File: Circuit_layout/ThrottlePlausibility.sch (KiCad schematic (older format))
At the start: 63 parts, among them SW1 TS5A3159-Q1, U1 ACPL-C870, U2 LM7810CT, U3 LM7805CT, U5 LM7332, U6 LM339, U8 74ACT11030

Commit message: added cap. info. for orders
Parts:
- removed C? (x9): 0.1u, symbol C
- added C? (x7): 0.1u, Capacitors_SMD:C_0805_HandSoldering, symbol C
- C?: footprint (none) -> Capacitors_SMD:C_0805_HandSoldering
- C?: footprint (none) -> Capacitors_SMD:C_0805_HandSoldering; Digikey P/N (none) -> 399-1168-1-ND; Man P/N (none) -> C0805C104K3RACTU; URL (none) -> http://www.digikey.com/product-detail/en/kemet/C0805C104K3R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
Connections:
- wire segments 168 -> 163
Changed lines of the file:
@@
 EESchema Schematic File Version 2
 LIBS:Circuit_layout-rescue
-LIBS:TSI_KiCad_Lib
 LIBS:TSI_HV_Isolater-cache
 LIBS:74xgxx
@@
 Wire Wire Line
 	5200 3700 5850 3700
-Wire Wire Line
-	5200 3900 5850 3900
-$Comp
-L C C?
-U 1 1 58ADD879
-P 5650 4200
-F 0 "C?" H 5675 4300 50  0000 L CNN
-F 1 "0.1u" H 5675 4100 50  0000 L CNN
-F 2 "" H 5688 4050 50  0000 C CNN
-F 3 "" H 5650 4200 50  0000 C CNN
-	1    5650 4200
-	1    0    0    -1
-$EndComp
-$Comp
-L C C?
-U 1 1 58ADD957
-P 5650 3400
-F 0 "C?" H 5675 3500 50  0000 L CNN
-F 1 "0.1u" H 5675 3300 50  0000 L CNN
-F 2 "" H 5688 3250 50  0000 C CNN
-F 3 "" H 5650 3400 50  0000 C CNN
-	1    5650 3400
-	1    0    0    -1
-$EndComp
 Text HLabel 3200 1700 0    60   Input ~ 0
 BP
@@
 F 0 "C?" H 11975 3600 50  0000 L CNN
 F 1 "DNP" H 11975 3400 50  0000 L CNN
-F 2 "" H 11988 3350 50  0000 C CNN
+F 2 "Capacitors_SMD:C_0805_HandSoldering" H 11988 3350 50  0001 C CNN
 F 3 "" H 11950 3500 50  0000 C CNN
 	1    11950 3500
@@
 	6150 3700 6400 3700
 Wire Wire Line
-	5650 3700 5650 3550
-Connection ~ 5650 3700
-Wire Wire Line
-	5650 4050 5650 3900
-Connection ~ 5650 3900
-Wire Wire Line
-	5650 3100 5650 3250
-Wire Wire Line
 	6300 3700 6300 3550
 Connection ~ 6300 3700
 Wire Wire Line
 	6300 3250 6300 3150
-Wire Wire Line
-	6300 3150 5650 3150
-Connection ~ 5650 3150
 $Comp
 L MCP6004 U?
@@
 F 0 "C?" H 3625 6850 50  0000 L CNN
 F 1 "0.1u" H 3625 6650 50  0000 L CNN
-F 2 "" H 3638 6600 50  0000 C CNN
-F 3 "" H 3600 6750 50  0000 C CNN
+F 2 "Capacitors_SMD:C_0805_HandSoldering" H 3638 6600 50  0001 C CNN
+F 3 "http://www.kemet.com/Lists/ProductCatalog/Attachments/53/KEM_C1002_X7R_SMD.pdf" H 3600 6750 50  0001 C CNN
+F 4 "399-1168-1-ND" H 3600 6750 60  0001 C CNN "Digikey P/N"
+F 5 "http://www.digikey.com/product-detail/en/kemet/C0805C104K3RACTU/399-1168-1-ND/411443" H 3600 6750 60  0001 C CNN "URL"
+F 6 "C0805C104K3RACTU" H 3600 6750 60  0001 C CNN "Man P/N"
 	1    3600 6750
-	1    0    0    -1
-$EndComp
-$Comp
-L C C?
-U 1 1 58AF6374
-P 3750 5950
-F 0 "C?" H 3775 6050 50  0000 L CNN
-F 1 "0.1u" H 3775 5850 50  0000 L CNN
-F 2 "" H 3788 5800 50  0000 C CNN
-F 3 "" H 3750 5950 50  0000 C CNN
-	1    3750 5950
 	1    0    0    -1
 $EndComp
@@
 	1    0    0    -1
 $EndComp
-Wire Wire Line
-	5650 4350 5650 4400
-$Comp
-L GND #PWR?
-U 1 1 58B314D0
-P 5650 4400
-F 0 "#PWR?" H 5650 4150 50  0001 C CNN
-F 1 "GND" H 5650 4250 50  0000 C CNN
-F 2 "" H 5650 4400 50  0000 C CNN
-F 3 "" H 5650 4400 50  0000 C CNN
-	1    5650 4400
-	1    0    0    -1
-$EndComp
 $Comp
 L GND #PWR?
 U 1 1 58B31589
-P 5650 3100
-F 0 "#PWR?" H 5650 2850 50  0001 C CNN
-F 1 "GND" H 5650 2950 50  0000 C CNN
-F 2 "" H 5650 3100 50  0000 C CNN
-F 3 "" H 5650 3100 50  0000 C CNN
-	1    5650 3100
+P 6300 3150
+F 0 "#PWR?" H 6300 2900 50  0001 C CNN
+F 1 "GND" H 6300 3000 50  0000 C CNN
+F 2 "" H 6300 3150 50  0000 C CNN
+F 3 "" H 6300 3150 50  0000 C CNN
+	1    6300 3150
 	1    0    0    1
 $EndComp
@@
 $EndComp
 $Comp
-L C C?
-U 1 1 58B3EF6F
-P 1650 2600
-F 0 "C?" H 1675 2700 50  0000 L CNN
-F 1 "0.1u" H 1675 2500 50  0000 L CNN
-F 2 "" H 1688 2450 50  0000 C CNN
-F 3 "" H 1650 2600 50  0000 C CNN
-	1    1650 2600
-	1    0    0    -1
-$EndComp
-$Comp
 L GND #PWR?
 U 1 1 58B3F616
@@
 Wire Wire Line
 	1550 1600 1850 1600
-$Comp
-L C C?
-U 1 1 58B403F1
-P 1650 1000
-F 0 "C?" H 1675 1100 50  0000 L CNN
-F 1 "0.1u" H 1675 900 50  0000 L CNN
-F 2 "" H 1688 850 50  0000 C CNN
-F 3 "" H 1650 1000 50  0000 C CNN
-	1    1650 1000
-	1    0    0    -1
-$EndComp
-$Comp
-L C C?
-U 1 1 58B404F5
-P 1650 1750
-F 0 "C?" H 1675 1850 50  0000 L CNN
-F 1 "0.1u" H 1675 1650 50  0000 L CNN
-F 2 "" H 1688 1600 50  0000 C CNN
-F 3 "" H 1650 1750 50  0000 C CNN
-	1    1650 1750
-	1    0    0    -1
-$EndComp
 Connection ~ 1650 1600
 Connection ~ 1650 850
@@
 Wire Wire Line
 	1550 3150 1850 3150
-$Comp
-L C C?
-U 1 1 58B47FEA
-P 1650 3300
-F 0 "C?" H 1675 3400 50  0000 L CNN
-F 1 "0.1u" H 1675 3200 50  0000 L CNN
-F 2 "" H 1688 3150 50  0000 C CNN
-F 3 "" H 1650 3300 50  0000 C CNN
-	1    1650 3300
-	1    0    0    -1
-$EndComp
 Connection ~ 1650 3150
 Text Label 1850 3150 0    60   ~ 0
@@
 Wire Wire Line
 	1550 3800 1850 3800
-$Comp
-L C C?
-U 1 1 58B4811B
-P 1650 3950
-F 0 "C?" H 1675 4050 50  0000 L CNN
-F 1 "0.1u" H 1675 3850 50  0000 L CNN
-F 2 "" H 1688 3800 50  0000 C CNN
-F 3 "" H 1650 3950 50  0000 C CNN
-	1    1650 3950
-	1    0    0    -1
-$EndComp
 Connection ~ 1650 3800
 Text Label 1850 3800 0    60   ~ 0
@@
 F 3 "" H 1650 4100 50  0000 C CNN
 	1    1650 4100
-	1    0    0    -1
-$EndComp
-$Comp
-L C C?
-U 1 1 58B49CCB
-P 3400 1000
-F 0 "C?" H 3425 1100 50  0000 L CNN
-F 1 "0.1u" H 3425 900 50  0000 L CNN
-F 2 "" H 3438 850 50  0000 C CNN
-F 3 "" H 3400 1000 50  0000 C CNN
-	1    3400 1000
 	1    0    0    -1
 $EndComp
@@
 	1    0    0    -1
 $EndComp
+$Comp
+L C C?
+U 1 1 58B3CEBF
+P 3750 5950
+F 0 "C?" H 3775 6050 50  0000 L CNN
+F 1 "0.1u" H 3775 5850 50  0000 L CNN
+F 2 "Capacitors_SMD:C_0805_HandSoldering" H 3788 5800 50  0001 C CNN
+F 3 "http://www.kemet.com/Lists/ProductCatalog/Attachments/53/KEM_C1002_X7R_SMD.pdf" H 3750 5950 50  0001 C CNN
+F 4 "399-1168-1-ND" H 3750 5950 60  0001 C CNN "Digikey P/N"
+F 5 "http://www.digikey.com/product-detail/en/kemet/C0805C104K3RACTU/399-1168-1-ND/411443" H 3750 5950 60  0001 C CNN "URL"
+F 6 "C0805C104K3RACTU" H 3750 5950 60  0001 C CNN "Man P/N"
+	1    3750 5950
+	1    0    0    -1
+$EndComp
+$Comp
+L C C?
+U 1 1 58B3FCB9
+P 1650 1000
+F 0 "C?" H 1675 1100 50  0000 L CNN
+F 1 "0.1u" H 1675 900 50  0000 L CNN
+F 2 "Capacitors_SMD:C_0805_HandSoldering" H 1688 850 50  0001 C CNN
+F 3 "http://www.kemet.com/Lists/ProductCatalog/Attachments/53/KEM_C1002_X7R_SMD.pdf" H 1650 1000 50  0001 C CNN
+F 4 "399-1168-1-ND" H 1650 1000 60  0001 C CNN "Digikey P/N"
+F 5 "http://www.digikey.com/product-detail/en/kemet/C0805C104K3RACTU/399-1168-1-ND/411443" H 1650 1000 60  0001 C CNN "URL"
+F 6 "C0805C104K3RACTU" H 1650 1000 60  0001 C CNN "Man P/N"
+	1    1650 1000
+	1    0    0    -1
+$EndComp
+$Comp
+L C C?
+U 1 1 58B3FDCB
+P 3400 1000
+F 0 "C?" H 3425 1100 50  0000 L CNN
+F 1 "0.1u" H 3425 900 50  0000 L CNN
+F 2 "Capacitors_SMD:C_0805_HandSoldering" H 3438 850 50  0001 C CNN
+F 3 "http://www.kemet.com/Lists/ProductCatalog/Attachments/53/KEM_C1002_X7R_SMD.pdf" H 3400 1000 50  0001 C CNN
+F 4 "399-1168-1-ND" H 3400 1000 60  0001 C CNN "Digikey P/N"
+F 5 "http://www.digikey.com/product-detail/en/kemet/C0805C104K3RACTU/399-1168-1-ND/411443" H 3400 1000 60  0001 C CNN "URL"
+F 6 "C0805C104K3RACTU" H 3400 1000 60  0001 C CNN "Man P/N"
+	1    3400 1000
+	1    0    0    -1
+$EndComp
+$Comp
+L C C?
+U 1 1 58B3FEBE
+P 1650 2600
+F 0 "C?" H 1675 2700 50  0000 L CNN
+F 1 "0.1u" H 1675 2500 50  0000 L CNN
+F 2 "Capacitors_SMD:C_0805_HandSoldering" H 1688 2450 50  0001 C CNN
+F 3 "http://www.kemet.com/Lists/ProductCatalog/Attachments/53/KEM_C1002_X7R_SMD.pdf" H 1650 2600 50  0001 C CNN
+F 4 "399-1168-1-ND" H 1650 2600 60  0001 C CNN "Digikey P/N"
+F 5 "http://www.digikey.com/product-detail/en/kemet/C0805C104K3RACTU/399-1168-1-ND/411443" H 1650 2600 60  0001 C CNN "URL"
+F 6 "C0805C104K3RACTU" H 1650 2600 60  0001 C CNN "Man P/N"
+	1    1650 2600
+	1    0    0    -1
+$EndComp
+$Comp
+L C C?
+U 1 1 58B3FFDC
+P 1650 1750
+F 0 "C?" H 1675 1850 50  0000 L CNN
+F 1 "0.1u" H 1675 1650 50  0000 L CNN
+F 2 "Capacitors_SMD:C_0805_HandSoldering" H 1688 1600 50  0001 C CNN
+F 3 "http://www.kemet.com/Lists/ProductCatalog/Attachments/53/KEM_C1002_X7R_SMD.pdf" H 1650 1750 50  0001 C CNN
+F 4 "399-1168-1-ND" H 1650 1750 60  0001 C CNN "Digikey P/N"
+F 5 "http://www.digikey.com/product-detail/en/kemet/C0805C104K3RACTU/399-1168-1-ND/411443" H 1650 1750 60  0001 C CNN "URL"
+F 6 "C0805C104K3RACTU" H 1650 1750 60  0001 C CNN "Man P/N"
+	1    1650 1750
+	1    0    0    -1
+$EndComp
+$Comp
+L C C?
+U 1 1 58B400E5
+P 1650 3300
+F 0 "C?" H 1675 3400 50  0000 L CNN
+F 1 "0.1u" H 1675 3200 50  0000 L CNN
+F 2 "Capacitors_SMD:C_0805_HandSoldering" H 1688 3150 50  0001 C CNN
+F 3 "http://www.kemet.com/Lists/ProductCatalog/Attachments/53/KEM_C1002_X7R_SMD.pdf" H 1650 3300 50  0001 C CNN
+F 4 "399-1168-1-ND" H 1650 3300 60  0001 C CNN "Digikey P/N"
+F 5 "http://www.digikey.com/product-detail/en/kemet/C0805C104K3RACTU/399-1168-1-ND/411443" H 1650 3300 60  0001 C CNN "URL"
+F 6 "C0805C104K3RACTU" H 1650 3300 60  0001 C CNN "Man P/N"
+	1    1650 3300
+	1    0    0    -1
+$EndComp
+$Comp
+L C C?
+U 1 1 58B40211
+P 1650 3950
+F 0 "C?" H 1675 4050 50  0000 L CNN
+F 1 "0.1u" H 1675 3850 50  0000 L CNN
+F 2 "Capacitors_SMD:C_0805_HandSoldering" H 1688 3800 50  0001 C CNN
+F 3 "http://www.kemet.com/Lists/ProductCatalog/Attachments/53/KEM_C1002_X7R_SMD.pdf" H 1650 3950 50  0001 C CNN
+F 4 "399-1168-1-ND" H 1650 3950 60  0001 C CNN "Digikey P/N"
+F 5 "http://www.digikey.com/product-detail/en/kemet/C0805C104K3RACTU/399-1168-1-ND/411443" H 1650 3950 60  0001 C CNN "URL"
+F 6 "C0805C104K3RACTU" H 1650 3950 60  0001 C CNN "Man P/N"
+	1    1650 3950
+	1    0    0    -1
+$EndComp
+Wire Wire Line
+	5200 3900 5850 3900
 $EndSCHEMATC

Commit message: KiCad BOM
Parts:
- gave numbers to parts that had none: 49

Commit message: finished adding footprints/info to all parts that I can
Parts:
- removed C21: 0.01u, Capacitors_SMD:C_0805_HandSoldering, symbol C
- removed R35, R36, R37, R39, R8: DNP, Resistors_SMD:R_0805_HandSoldering, symbol R
- added C?: 0.01u, Capacitors_SMD:C_0805_HandSoldering, symbol C
- added R? (x4): 499, Resistors_SMD:R_0805_HandSoldering, symbol R
- added R?: 9.31k, Resistors_SMD:R_0805_HandSoldering, symbol R
- C20: Digikey P/N (none) -> 399-1158-1-ND; Man P/N (none) -> C0805C103K5RACTU; URL (none) -> http://www.digikey.com/product-detail/en/kemet/C0805C103K5R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
- R38: value DNP -> 9.31k; Digikey P/N (none) -> P9.31KCCT-ND; Man P/N (none) -> ERJ-6ENF9311V; URL (none) -> http://www.digikey.com/product-detail/en/panasonic-electron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
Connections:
- net labels added: Brake_5, Throttle_PL
- net labels removed: BRAKE_5
- wire segments 163 -> 165
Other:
- note added: "Open/Short Window\n(90% travel)"
- note added: "Resistors Set for maximum\nof 90% travel ( > will trigger fault)"
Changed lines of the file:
@@
 EESchema Schematic File Version 2
 LIBS:Circuit_layout-rescue
-LIBS:TSI_KiCad_Lib
 LIBS:TSI_HV_Isolater-cache
 LIBS:74xgxx
@@
 Comment4 "DEVELOPMENT ONLY"
 $EndDescr
-$Comp
-L R R8
-U 1 1 58A60010
-P 7450 5400
-F 0 "R8" V 7530 5400 50  0000 C CNN
-F 1 "DNP" V 7450 5400 50  0000 C CNN
-F 2 "Resistors_SMD:R_0805_HandSoldering" V 7380 5400 50  0001 C CNN
-F 3 "" H 7450 5400 50  0000 C CNN
-	1    7450 5400
-	1    0    0    -1
-$EndComp
 Text Label 6300 6300 0    60   ~ 0
 APPS1_ISO
@@
 BP
 Text HLabel 1500 2450 0    60   Output ~ 0
-BRAKE_5
+Brake_5
 Text HLabel 3200 1950 0    60   Input ~ 0
 BP_uC
@@
 F 1 "0.01u" H 10675 7250 50  0000 L CNN
 F 2 "Capacitors_SMD:C_0805_HandSoldering" H 10688 7200 50  0001 C CNN
-F 3 "" H 10650 7350 50  0000 C CNN
+F 3 "http://www.kemet.com/Lists/ProductCatalog/Attachments/53/KEM_C1002_X7R_SMD.pdf" H 10650 7350 50  0001 C CNN
+F 4 "399-1158-1-ND" H 10650 7350 60  0001 C CNN "Digikey P/N"
+F 5 "http://www.digikey.com/product-detail/en/kemet/C0805C103K5RACTU/399-1158-1-ND/411433" H 10650 7350 60  0001 C CNN "URL"
+F 6 "C0805C103K5RACTU" H 10650 7350 60  0001 C CNN "Man P/N"
 	1    10650 7350
 	1    0    0    -1
@@
 $EndComp
 Wire Wire Line
-	1500 2450 1650 2450
+	1500 2450 1850 2450
 Wire Wire Line
 	1650 2450 1650 2350
@@
 	1    12950 7000
 	1    0    0    -1
-$EndComp
-$Comp
-L C C21
-U 1 1 58B5CCC9
-P 11600 6750
-F 0 "C21" H 11625 6850 50  0000 L CNN
-F 1 "0.01u" H 11625 6650 50  0000 L CNN
-F 2 "Capacitors_SMD:C_0805_HandSoldering" H 11638 6600 50  0001 C CNN
-F 3 "" H 11600 6750 50  0000 C CNN
-	1    11600 6750
-	0    1    1    0
 $EndComp
 $Comp
@@
 $EndComp
 $Comp
-L R R35
-U 1 1 58B77D1A
-P 7450 6300
-F 0 "R35" V 7530 6300 50  0000 C CNN
-F 1 "DNP" V 7450 6300 50  0000 C CNN
-F 2 "Resistors_SMD:R_0805_HandSoldering" V 7380 6300 50  0001 C CNN
-F 3 "" H 7450 6300 50  0000 C CNN
-	1    7450 6300
-	1    0    0    -1
-$EndComp
-$Comp
-L R R36
-U 1 1 58B77E07
-P 7450 7200
-F 0 "R36" V 7530 7200 50  0000 C CNN
-F 1 "DNP" V 7450 7200 50  0000 C CNN
-F 2 "Resistors_SMD:R_0805_HandSoldering" V 7380 7200 50  0001 C CNN
-F 3 "" H 7450 7200 50  0000 C CNN
-	1    7450 7200
-	1    0    0    -1
-$EndComp
-$Comp
-L R R37
-U 1 1 58B77FF9
-P 7450 7950
-F 0 "R37" V 7530 7950 50  0000 C CNN
-F 1 "DNP" V 7450 7950 50  0000 C CNN
-F 2 "Resistors_SMD:R_0805_HandSoldering" V 7380 7950 50  0001 C CNN
-F 3 "" H 7450 7950 50  0000 C CNN
-	1    7450 7950
-	1    0    0    -1
-$EndComp
-$Comp
 L R R38
 U 1 1 58B780F8
 P 7450 8850
 F 0 "R38" V 7530 8850 50  0000 C CNN
-F 1 "DNP" V 7450 8850 50  0000 C CNN
+F 1 "9.31k" V 7450 8850 50  0000 C CNN
 F 2 "Resistors_SMD:R_0805_HandSoldering" V 7380 8850 50  0001 C CNN
-F 3 "" H 7450 8850 50  0000 C CNN
+F 3 "https://industrial.panasonic.com/ww/products/resistors/chip-resistors/general-purpose-chip-resistors/precision-thick-film-chip-resistors/ERJ6ENF9311V" H 7450 8850 50  0001 C CNN
+F 4 "P9.31KCCT-ND" V 7450 8850 60  0001 C CNN "Digikey P/N"
+F 5 "http://www.digikey.com/product-detail/en/panasonic-electronic-components/ERJ-6ENF9311V/P9.31KCCT-ND/119238" V 7450 8850 60  0001 C CNN "URL"
+F 6 "ERJ-6ENF9311V" V 7450 8850 60  0001 C CNN "Man P/N"
 	1    7450 8850
-	1    0    0    -1
-$EndComp
-$Comp
-L R R39
-U 1 1 58B78272
-P 7450 9750
-F 0 "R39" V 7530 9750 50  0000 C CNN
-F 1 "DNP" V 7450 9750 50  0000 C CNN
-F 2 "Resistors_SMD:R_0805_HandSoldering" V 7380 9750 50  0001 C CNN
-F 3 "" H 7450 9750 50  0000 C CNN
-	1    7450 9750
 	1    0    0    -1
 $EndComp
@@
 Wire Wire Line
 	5200 3900 5850 3900
+$Comp
+L C C?
+U 1 1 58B382BA
+P 11650 6750
+F 0 "C?" H 11675 6850 50  0000 L CNN
+F 1 "0.01u" H 11675 6650 50  0000 L CNN
+F 2 "Capacitors_SMD:C_0805_HandSoldering" H 11688 6600 50  0001 C CNN
+F 3 "http://www.kemet.com/Lists/ProductCatalog/Attachments/53/KEM_C1002_X7R_SMD.pdf" H 11650 6750 50  0001 C CNN
+F 4 "399-1158-1-ND" H 11650 6750 60  0001 C CNN "Digikey P/N"
+F 5 "http://www.digikey.com/product-detail/en/kemet/C0805C103K5RACTU/399-1158-1-ND/411433" H 11650 6750 60  0001 C CNN "URL"
+F 6 "C0805C103K5RACTU" H 11650 6750 60  0001 C CNN "Man P/N"
+	1    11650 6750
+	0    1    1    0
+$EndComp
+Text Notes 5950 7650 0    60   ~ 0
+Resistors Set for maximum\nof 90% travel ( > will trigger fault)
+Text Notes 5750 5900 0    99   ~ 0
+Open/Short Window\n(90% travel)
+$Comp
+L R R?
+U 1 1 58B3D937
+P 7450 5400
+F 0 "R?" V 7530 5400 50  0000 C CNN
+F 1 "499" V 7450 5400 50  0000 C CNN
+F 2 "Resistors_SMD:R_0805_HandSoldering" V 7380 5400 50  0001 C CNN
+F 3 "" H 7450 5400 50  0000 C CNN
+F 4 "P499DACT-ND" V 7450 5400 60  0001 C CNN "DigiKey P/N"
+F 5 "http://www.digikey.com/product-detail/en/panasonic-electronic-components/ERA-6AEB4990V/P499DACT-ND/3075160" V 7450 5400 60  0001 C CNN "URL"
+F 6 "ERA-6AEB4990V" V 7450 5400 60  0001 C CNN "Man P/N"
+	1    7450 5400
+	-1   0    0    1
+$EndComp
+$Comp
+L R R?
+U 1 1 58B3DA61
+P 7450 7200
+F 0 "R?" V 7530 7200 50  0000 C CNN
+F 1 "499" V 7450 7200 50  0000 C CNN
+F 2 "Resistors_SMD:R_0805_HandSoldering" V 7380 7200 50  0001 C CNN
+F 3 "" H 7450 7200 50  0000 C CNN
+F 4 "P499DACT-ND" V 7450 7200 60  0001 C CNN "DigiKey P/N"
+F 5 "http://www.digikey.com/product-detail/en/panasonic-electronic-components/ERA-6AEB4990V/P499DACT-ND/3075160" V 7450 7200 60  0001 C CNN "URL"
+F 6 "ERA-6AEB4990V" V 7450 7200 60  0001 C CNN "Man P/N"
+	1    7450 7200
+	-1   0    0    1
+$EndComp
+$Comp
+L R R?
+U 1 1 58B3DB76
+P 7450 7950
+F 0 "R?" V 7530 7950 50  0000 C CNN
+F 1 "499" V 7450 7950 50  0000 C CNN
+F 2 "Resistors_SMD:R_0805_HandSoldering" V 7380 7950 50  0001 C CNN
+F 3 "" H 7450 7950 50  0000 C CNN
+F 4 "P499DACT-ND" V 7450 7950 60  0001 C CNN "DigiKey P/N"
+F 5 "http://www.digikey.com/product-detail/en/panasonic-electronic-components/ERA-6AEB4990V/P499DACT-ND/3075160" V 7450 7950 60  0001 C CNN "URL"
+F 6 "ERA-6AEB4990V" V 7450 7950 60  0001 C CNN "Man P/N"
+	1    7450 7950
+	-1   0    0    1
+$EndComp
+$Comp
+L R R?
+U 1 1 58B3DC82
+P 7450 9750
+F 0 "R?" V 7530 9750 50  0000 C CNN
+F 1 "499" V 7450 9750 50  0000 C CNN
+F 2 "Resistors_SMD:R_0805_HandSoldering" V 7380 9750 50  0001 C CNN
+F 3 "" H 7450 9750 50  0000 C CNN
+F 4 "P499DACT-ND" V 7450 9750 60  0001 C CNN "DigiKey P/N"
+F 5 "http://www.digikey.com/product-detail/en/panasonic-electronic-components/ERA-6AEB4990V/P499DACT-ND/3075160" V 7450 9750 60  0001 C CNN "URL"
+F 6 "ERA-6AEB4990V" V 7450 9750 60  0001 C CNN "Man P/N"
+	1    7450 9750
+	-1   0    0    1
+$EndComp
+$Comp
+L R R?
+U 1 1 58B3E84B
+P 7450 6300
+F 0 "R?" V 7530 6300 50  0000 C CNN
+F 1 "9.31k" V 7450 6300 50  0000 C CNN
+F 2 "Resistors_SMD:R_0805_HandSoldering" V 7380 6300 50  0001 C CNN
+F 3 "https://industrial.panasonic.com/ww/products/resistors/chip-resistors/general-purpose-chip-resistors/precision-thick-film-chip-resistors/ERJ6ENF9311V" H 7450 6300 50  0001 C CNN
+F 4 "P9.31KCCT-ND" V 7450 6300 60  0001 C CNN "Digikey P/N"
+F 5 "http://www.digikey.com/product-detail/en/panasonic-electronic-components/ERJ-6ENF9311V/P9.31KCCT-ND/119238" V 7450 6300 60  0001 C CNN "URL"
+F 6 "ERJ-6ENF9311V" V 7450 6300 60  0001 C CNN "Man P/N"
+	1    7450 6300
+	1    0    0    -1
+$EndComp
+Connection ~ 1650 2450
+Text Label 1850 2450 0    60   ~ 0
+APPS_5
+Text HLabel 3200 2900 0    60   Output ~ 0
+Throttle_PL
+Wire Wire Line
+	3200 2900 3400 2900
+Text Label 3400 2900 0    60   ~ 0
+Throttle_PL
+Wire Wire Line
+	10400 6300 10600 6300
+Text Label 10600 6300 0    60   ~ 0
+Throttle_PL
 $EndSCHEMATC

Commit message: took notes w/ greg
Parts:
- gave numbers to parts that had none: 6
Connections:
- net labels removed: +10V

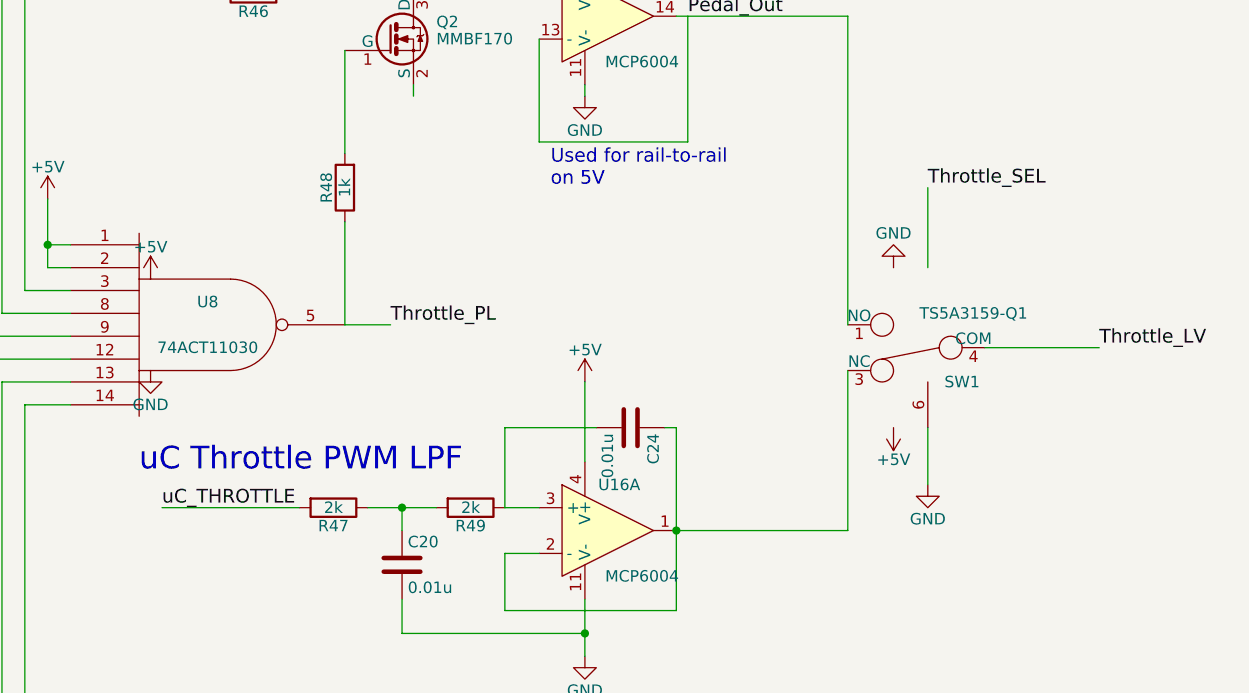
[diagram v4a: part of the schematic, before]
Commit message: got rid of some warnings with nets.
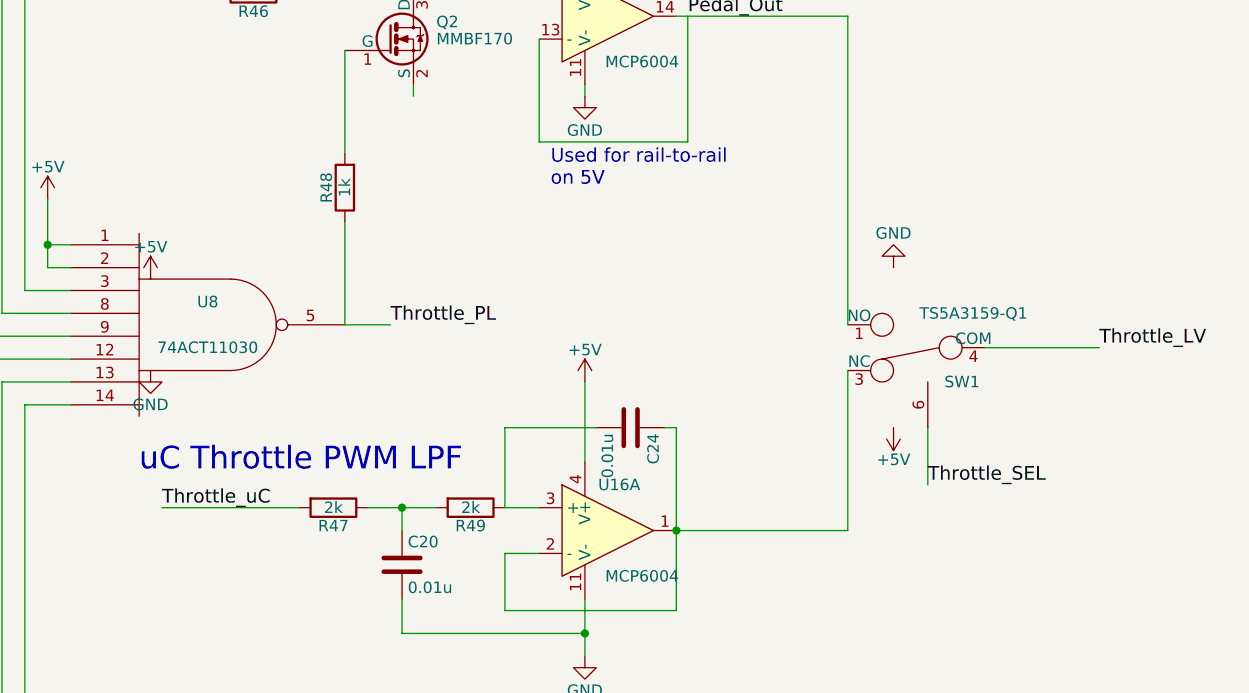
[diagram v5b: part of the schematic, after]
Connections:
- net uC_THROTTLE is gone; now on net Throttle_uC: R47.2
- net GND: no longer SW1.6
- net Throttle_SEL: now also SW1.6
